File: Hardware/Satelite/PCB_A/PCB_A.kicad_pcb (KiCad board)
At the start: 2 copper layers, 47 x 47 mm, 40 parts, among them J1 Batería LiPo (Soldada), J2 CONUFL001-SMD, J3 Servo Globo, J4 Conector_PCB_A-B, J5 Servo Paracaídas, Q1 SSM3J338R,LF, U1 A2235-H, U2 CC1101RGP, U3 0915BM15A0001E, Y1 26 MHz

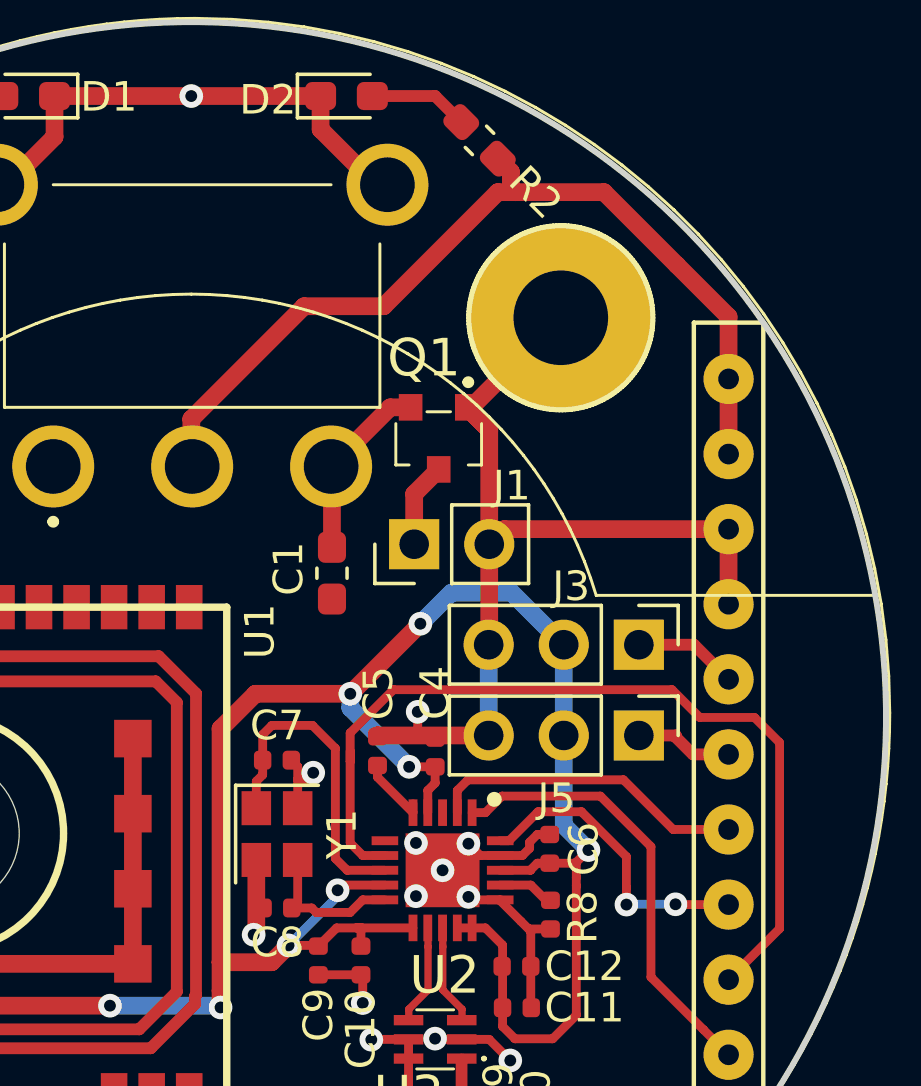
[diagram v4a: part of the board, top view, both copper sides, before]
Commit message: Trazas más gruesas para VBat y corrección de error DRC en PCB_A
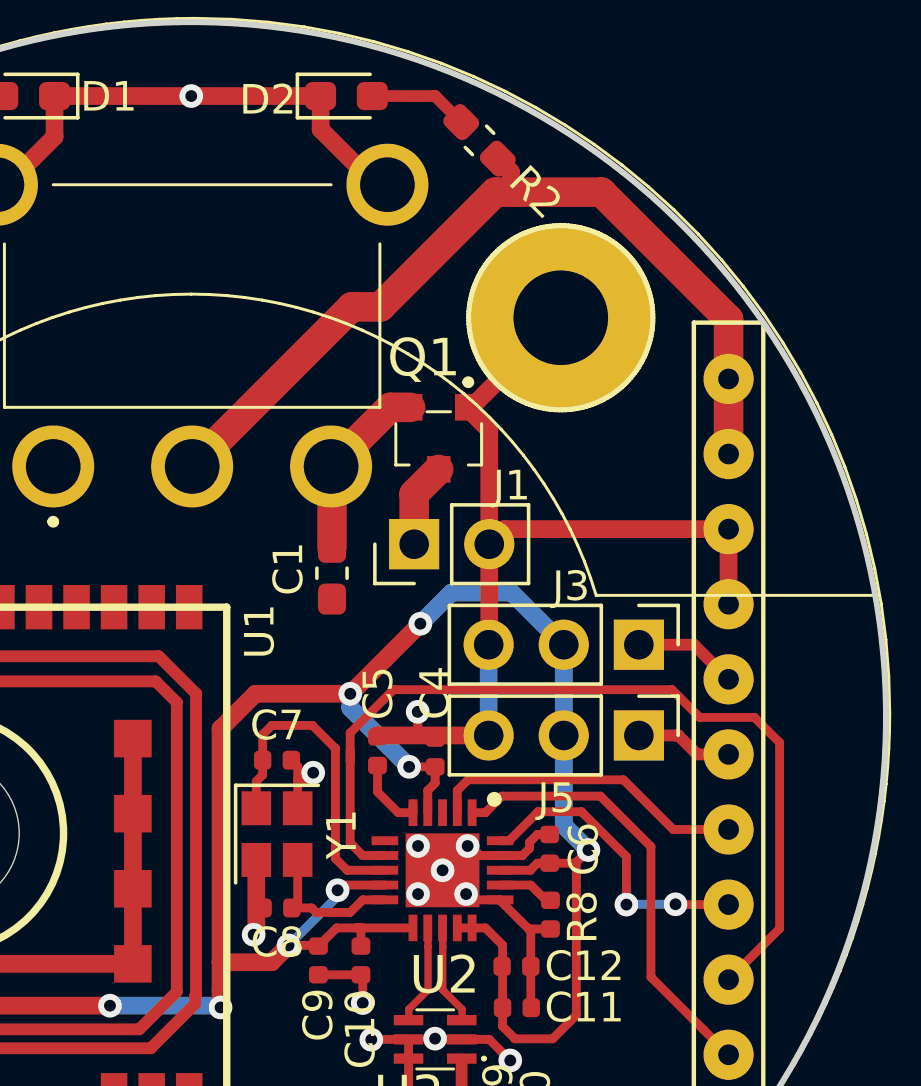
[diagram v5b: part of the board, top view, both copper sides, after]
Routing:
- net Net-(J4-Pad1): track 31.1 -> 29.7 mm
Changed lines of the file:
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@@
     (thickness 1.6)
     (drawings 1)
-    (tracks 332)
+    (tracks 331)
     (zones 0)
     (modules 40)
@@
   )
   (gr_circle (center 0 0) (end 23.5 0) (layer Edge.Cuts) (width 0.2))
-  (segment (start 9.1432 11.5886) (end 9.1432 12.8816) (width 0.4) (layer F.Cu) (net 48))
-  (segment (start 7.3582 9.8886) (end 8.0082 9.2386) (width 0.25) (layer F.Cu) (net 51))
-  (segment (start 8.0082 9.2386) (end 8.0082 7.7732) (width 0.25) (layer F.Cu) (net 51))
-  (segment (start 8.0082 7.7732) (end 8.0082 7.1232) (width 0.25) (layer F.Cu) (net 51))
-  (segment (start 7.3582 10.2636) (end 7.3582 9.8886) (width 0.25) (layer F.Cu) (net 51))
-  (segment (start 8.5082 7.7732) (end 8.5082 7.1232) (width 0.25) (layer F.Cu) (net 52))
-  (segment (start 9.1582 10.2636) (end 9.1582 9.8886) (width 0.25) (layer F.Cu) (net 52))
-  (segment (start 9.1582 9.8886) (end 8.5082 9.2386) (width 0.25) (layer F.Cu) (net 52))
-  (segment (start 8.5082 9.2386) (end 8.5082 7.7732) (width 0.25) (layer F.Cu) (net 52))
   (via (at 8.5 5.19) (size 0.8) (drill 0.4) (layers F.Cu B.Cu) (net 1))
-  (via (at 7.6 6.065) (size 0.8) (drill 0.4) (layers F.Cu B.Cu) (net 1))
-  (via (at 7.6 4.265) (size 0.8) (drill 0.4) (layers F.Cu B.Cu) (net 1))
-  (via (at 9.375 6.09) (size 0.8) (drill 0.4) (layers F.Cu B.Cu) (net 1))
-  (via (at 9.375 4.29) (size 0.8) (drill 0.4) (layers F.Cu B.Cu) (net 1))
+  (via (at 7.6708 5.9944) (size 0.8) (drill 0.4) (layers F.Cu B.Cu) (net 1))
+  (via (at 7.6708 4.3688) (size 0.8) (drill 0.4) (layers F.Cu B.Cu) (net 1))
+  (via (at 9.2964 5.9944) (size 0.8) (drill 0.4) (layers F.Cu B.Cu) (net 1))
+  (via (at 9.3472 4.3688) (size 0.8) (drill 0.4) (layers F.Cu B.Cu) (net 1))
   (segment (start -12.75 -13.25) (end -12.5 -13.5) (width 0.4) (layer F.Cu) (net 1))
   (segment (start -12.75 -7.875) (end -12.75 -13.25) (width 0.4) (layer F.Cu) (net 1))
@@
   (segment (start 5.14 -8.88) (end 4.73 -8.47) (width 0.6) (layer F.Cu) (net 2))
   (segment (start 4.76 -8.44) (end 4.73 -8.47) (width 0.6) (layer F.Cu) (net 2))
-  (segment (start 4.76 -5.735) (end 4.76 -8.44) (width 0.6) (layer F.Cu) (net 2))
-  (segment (start 6.73 -10.47) (end 4.73 -8.47) (width 0.6) (layer F.Cu) (net 2))
-  (segment (start 7.42 -10.47) (end 6.73 -10.47) (width 0.6) (layer F.Cu) (net 2))
+  (segment (start 4.76 -5.735) (end 4.76 -8.44) (width 1) (layer F.Cu) (net 2))
+  (segment (start 6.73 -10.47) (end 4.73 -8.47) (width 1) (layer F.Cu) (net 2))
+  (segment (start 7.42 -10.47) (end 6.73 -10.47) (width 1) (layer F.Cu) (net 2))
   (segment (start -18.175 1.27) (end -16.53 1.27) (width 0.6) (layer F.Cu) (net 3))
   (segment (start -16.53 1.27) (end -15.325 2.475) (width 0.6) (layer F.Cu) (net 3))
@@
   (segment (start 8.25 -21) (end 9.131282 -20.118718) (width 0.4) (layer F.Cu) (net 5))
   (segment (start 6.125 -21) (end 8.25 -21) (width 0.4) (layer F.Cu) (net 5))
-  (segment (start 7.54 -7.54) (end 8.37 -8.37) (width 0.6) (layer F.Cu) (net 6))
-  (segment (start 7.54 -5.84) (end 7.54 -7.54) (width 0.6) (layer F.Cu) (net 6))
+  (segment (start 7.54 -7.54) (end 8.37 -8.37) (width 1) (layer F.Cu) (net 6))
+  (segment (start 7.54 -5.84) (end 7.54 -7.54) (width 1) (layer F.Cu) (net 6))
   (segment (start 17.005 -2.44) (end 15.14 -2.44) (width 0.4) (layer F.Cu) (net 7))
   (segment (start 18.175 -1.27) (end 17.005 -2.44) (width 0.4) (layer F.Cu) (net 7))
@@
   (segment (start 14.62 2.13) (end 16.3 3.81) (width 0.3) (layer F.Cu) (net 16))
   (segment (start 16.39 0.63) (end 15.14 0.63) (width 0.4) (layer F.Cu) (net 17))
-  (segment (start 16.39 0.687081) (end 16.39 0.63) (width 0.4) (layer F.Cu) (net 17))
-  (segment (start 16.972919 1.27) (end 16.39 0.687081) (width 0.4) (layer F.Cu) (net 17))
-  (segment (start 18.175 1.27) (end 16.972919 1.27) (width 0.4) (layer F.Cu) (net 17))
+  (segment (start 16.4796 0.63) (end 16.39 0.63) (width 0.4) (layer F.Cu) (net 17))
+  (segment (start 18.175 1.27) (end 17.1196 1.27) (width 0.4) (layer F.Cu) (net 17))
+  (segment (start 17.1196 1.27) (end 16.4796 0.63) (width 0.4) (layer F.Cu) (net 17))
   (segment (start 5.8 4.69) (end 5.37501 4.26501) (width 0.3) (layer F.Cu) (net 18))
   (segment (start 6.55 4.69) (end 5.8 4.69) (width 0.3) (layer F.Cu) (net 18))
@@
   (segment (start 15.55 4.39) (end 15.55 8.805) (width 0.3) (layer F.Cu) (net 20))
   (segment (start 15.55 8.805) (end 17.325001 10.580001) (width 0.3) (layer F.Cu) (net 20))
-  (segment (start 18.175 -8.89) (end 18.175 -13.535) (width 0.6) (layer F.Cu) (net 21))
-  (segment (start 0 -10.072221) (end 3.817779 -13.89) (width 0.6) (layer F.Cu) (net 21))
-  (segment (start 0 -8.11) (end 0 -10.072221) (width 0.6) (layer F.Cu) (net 21))
-  (segment (start 3.817779 -13.89) (end 6.51 -13.89) (width 0.6) (layer F.Cu) (net 21))
-  (segment (start 6.51 -13.89) (end 10.368718 -17.748718) (width 0.6) (layer F.Cu) (net 21))
-  (segment (start 13.961282 -17.748718) (end 16.43 -15.28) (width 0.6) (layer F.Cu) (net 21))
-  (segment (start 18.175 -13.535) (end 16.43 -15.28) (width 0.6) (layer F.Cu) (net 21))
   (segment (start 10.810659 -17.908059) (end 10.97 -17.748718) (width 0.6) (layer F.Cu) (net 21))
   (segment (start 10.810659 -18.439341) (end 10.810659 -17.908059) (width 0.6) (layer F.Cu) (net 21))
   (segment (start 10.368718 -18.881282) (end 10.810659 -18.439341) (width 0.6) (layer F.Cu) (net 21))
-  (segment (start 10.368718 -17.748718) (end 10.97 -17.748718) (width 0.6) (layer F.Cu) (net 21))
-  (segment (start 10.97 -17.748718) (end 13.961282 -17.748718) (width 0.6) (layer F.Cu) (net 21))
+  (segment (start 13.875284 -17.748718) (end 10.97 -17.748718) (width 1) (layer F.Cu) (net 21))
+  (segment (start 18.175 -13.449002) (end 13.875284 -17.748718) (width 1) (layer F.Cu) (net 21))
+  (segment (start 18.175 -8.89) (end 18.175 -13.449002) (width 1) (layer F.Cu) (net 21))
+  (segment (start 5.4284 -13.8684) (end 0.03 -8.47) (width 1) (layer F.Cu) (net 21))
+  (segment (start 6.4008 -13.8684) (end 5.4284 -13.8684) (width 1) (layer F.Cu) (net 21))
+  (segment (start 10.97 -17.748718) (end 10.281118 -17.748718) (width 1) (layer F.Cu) (net 21))
+  (segment (start 10.281118 -17.748718) (end 6.4008 -13.8684) (width 1) (layer F.Cu) (net 21))
   (segment (start -15.31 14.265) (end -14.6 14.975) (width 0.4) (layer F.Cu) (net 22))
   (segment (start -15.31 12.8) (end -15.31 14.265) (width 0.4) (layer F.Cu) (net 22))
@@
   (segment (start -0.49 -0.49) (end -1.2 -1.2) (width 0.4) (layer F.Cu) (net 29))
   (segment (start 7.5 3.24) (end 7.5 2.94) (width 0.3) (layer F.Cu) (net 41))
-  (segment (start 6.3 1.645) (end 6.3 2.04) (width 0.3) (layer F.Cu) (net 41))
-  (segment (start 6.3 2.04) (end 7.5 3.24) (width 0.3) (layer F.Cu) (net 41))
+  (segment (start 6.9992 3.24) (end 7.5 3.24) (width 0.3) (layer F.Cu) (net 41))
+  (segment (start 6.3 1.645) (end 6.3 2.5408) (width 0.3) (layer F.Cu) (net 41))
+  (segment (start 6.3 2.5408) (end 6.9992 3.24) (width 0.3) (layer F.Cu) (net 41))
   (segment (start 5.275 5.19) (end 6.55 5.19) (width 0.3) (layer F.Cu) (net 42))
   (segment (start 4.875 4.79) (end 5.275 5.19) (width 0.3) (layer F.Cu) (net 42))
@@
   (segment (start 11.485 5.69) (end 12 6.205) (width 0.3) (layer F.Cu) (net 47))
   (segment (start 10.45 5.69) (end 11.485 5.69) (width 0.3) (layer F.Cu) (net 47))
+  (segment (start 9.1432 11.5886) (end 9.1432 12.8816) (width 0.4) (layer F.Cu) (net 48))
+  (segment (start 7.3582 9.8886) (end 8.0082 9.2386) (width 0.25) (layer F.Cu) (net 51))
+  (segment (start 8.0082 9.2386) (end 8.0082 7.7732) (width 0.25) (layer F.Cu) (net 51))
+  (segment (start 8.0082 7.7732) (end 8.0082 7.1232) (width 0.25) (layer F.Cu) (net 51))
+  (segment (start 7.3582 10.2636) (end 7.3582 9.8886) (width 0.25) (layer F.Cu) (net 51))
+  (segment (start 8.5082 7.7732) (end 8.5082 7.1232) (width 0.25) (layer F.Cu) (net 52))
+  (segment (start 9.1582 10.2636) (end 9.1582 9.8886) (width 0.25) (layer F.Cu) (net 52))
+  (segment (start 9.1582 9.8886) (end 8.5082 9.2386) (width 0.25) (layer F.Cu) (net 52))
+  (segment (start 8.5082 9.2386) (end 8.5082 7.7732) (width 0.25) (layer F.Cu) (net 52))
   (zone (net 1) (net_name GND) (layer F.Cu) (hatch edge 0.508)
     (connect_pads (clearance 0.508))

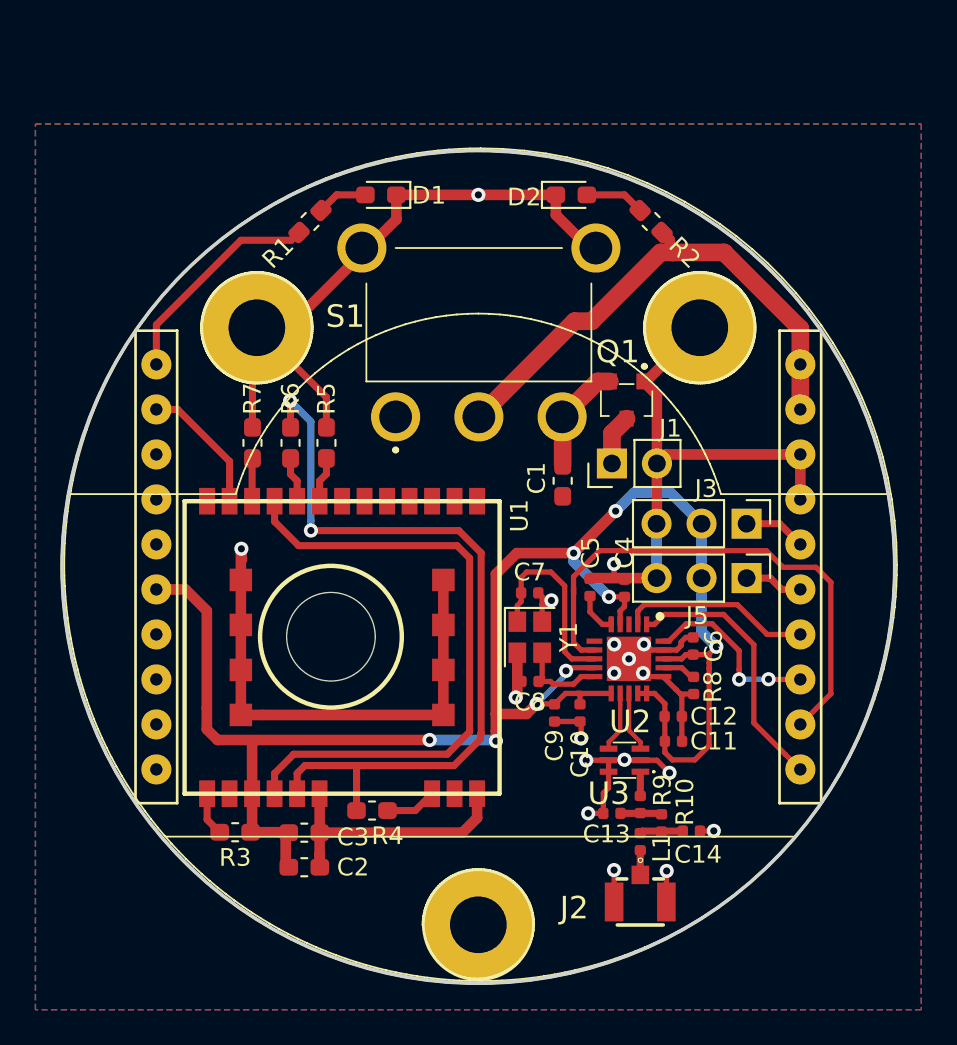
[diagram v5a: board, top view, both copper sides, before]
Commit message: Servos alimentados con 5V internos del conector A-B
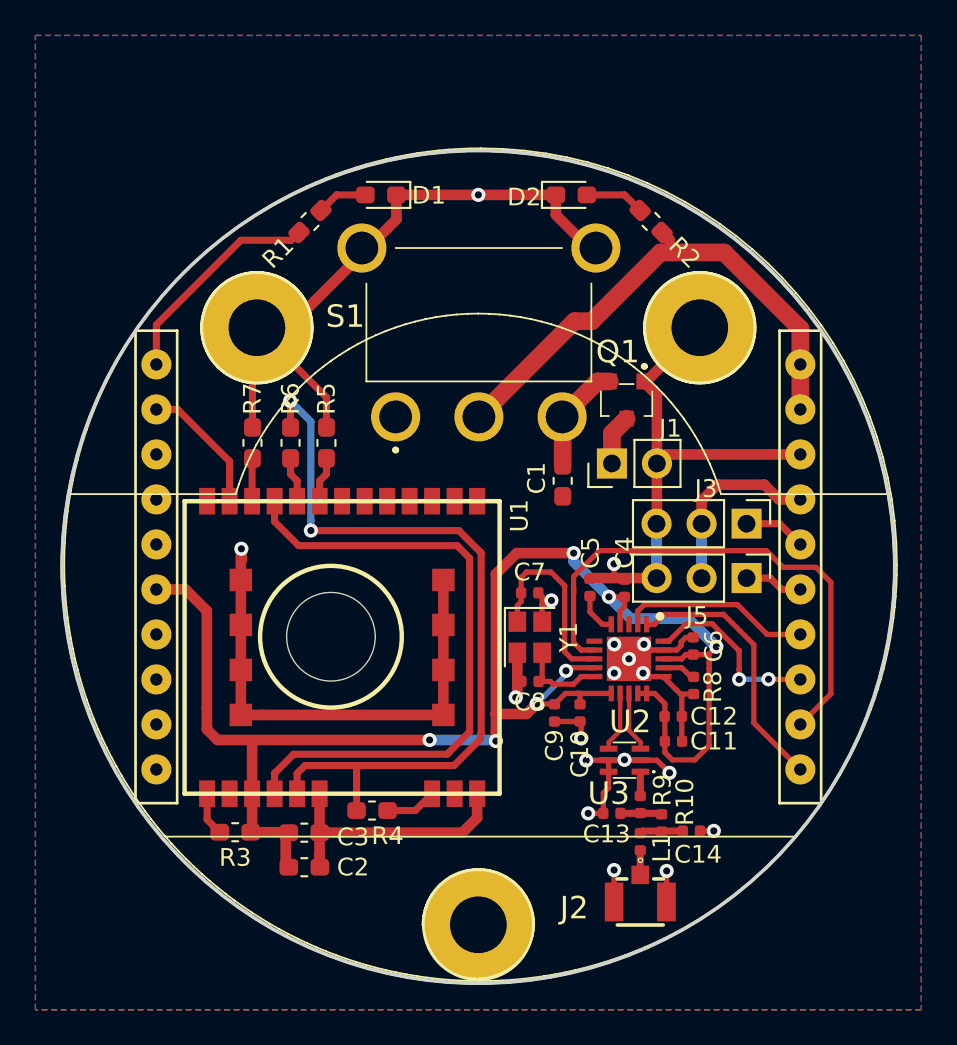
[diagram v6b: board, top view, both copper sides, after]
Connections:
- J3 pad 2: +3V3_Internal -> +5V
- J4 pad 15: Net-(J4-Pad15) -> GND
- J4 pad 4: GND -> +5V
- J5 pad 2: +3V3_Internal -> +5V
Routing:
- net +5V: track 0.00 -> 10.7 mm
- net +3V3_Internal: track 100.7 -> 92.4 mm, vias 8 -> 7
- net GND: track 145.3 -> 142.7 mm

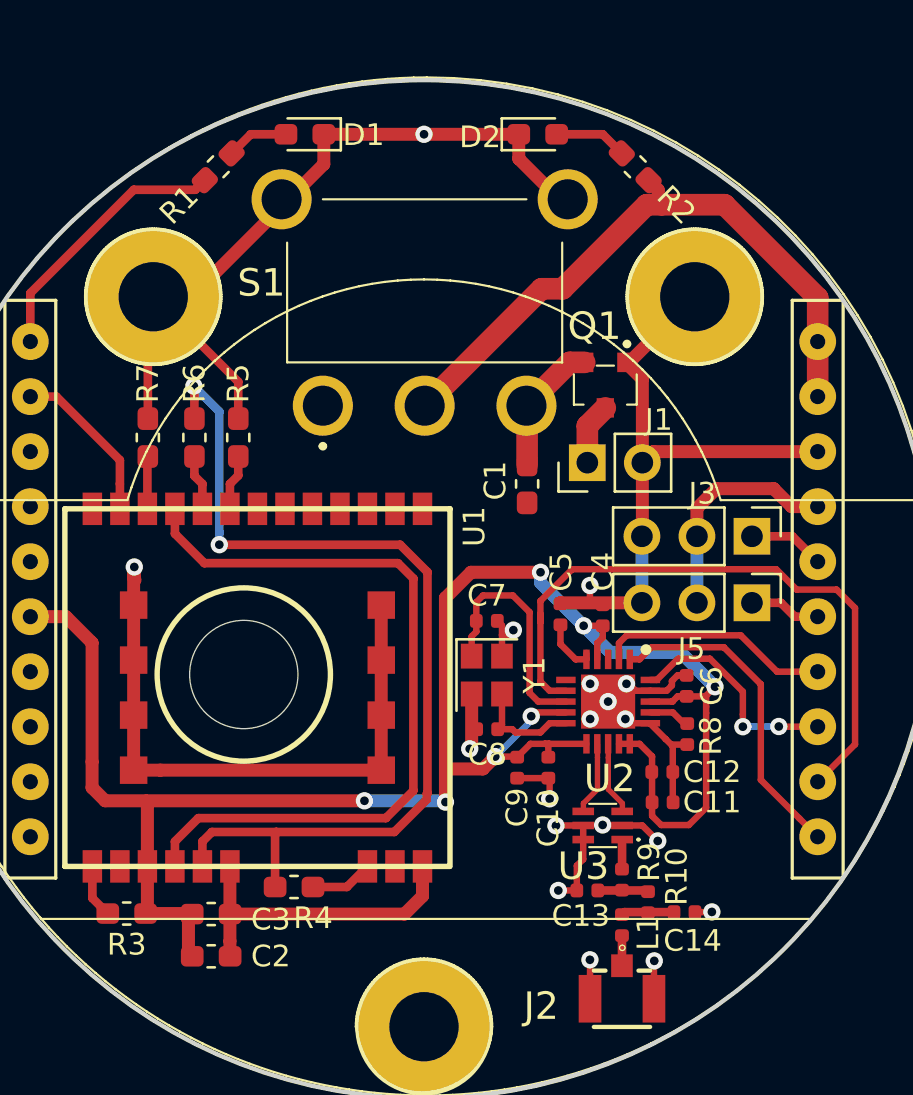
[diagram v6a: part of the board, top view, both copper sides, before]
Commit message: Reducido el díametro de vías de 0.4 a 0.3 en PCB_A
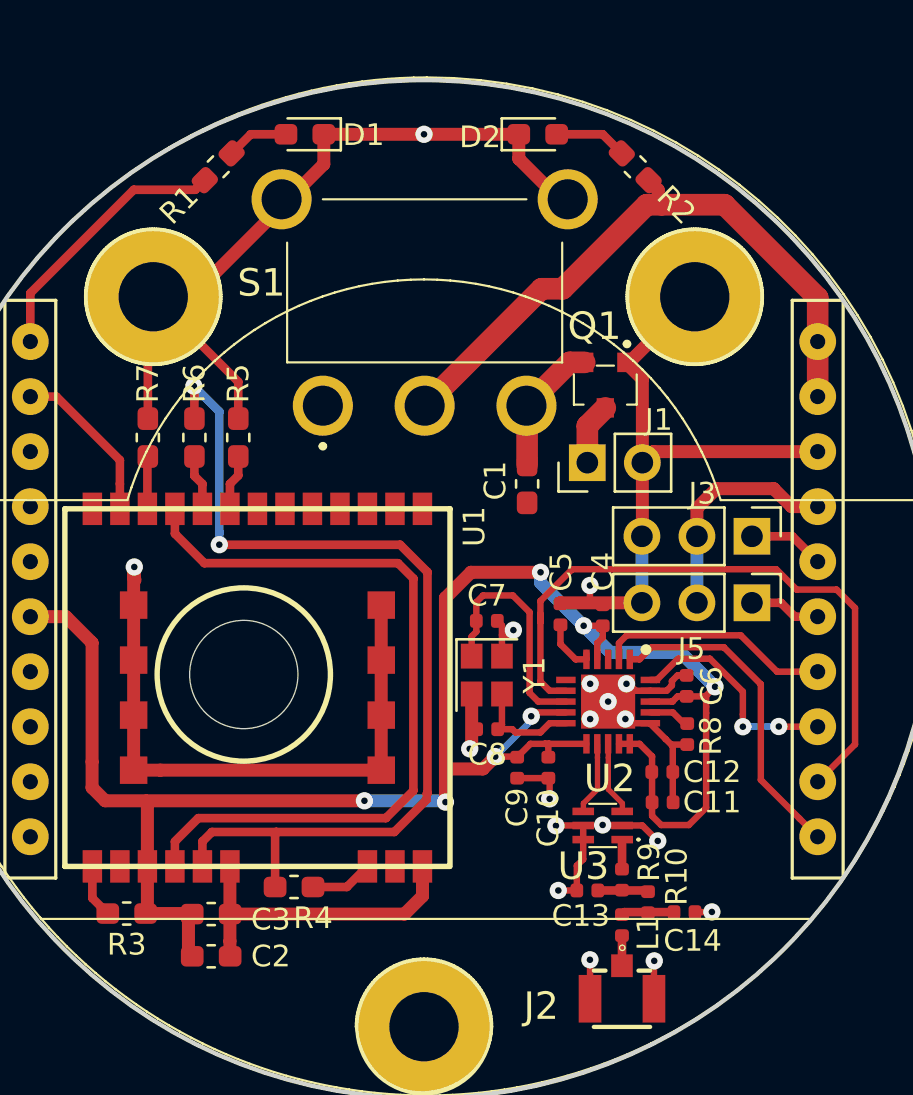
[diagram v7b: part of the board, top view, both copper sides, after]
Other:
- net class ANT: via_drill 0.4 -> 0.3
- net class Alimentacion: via_drill 0.4 -> 0.3
- net class Default: via_drill 0.4 -> 0.3
- net class RF_DIF: via_drill 0.4 -> 0.3

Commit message: PCB_A terminado
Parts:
- added REF**: PCB_mayor_diametro, AXTEC:PCB_mayor_diametro, F.Cu at (0.00, 0.00)
- moved J5 5.79 mm to (20.9, 0.00), turned to 0 degrees
- moved C9 2.82 mm to (6.90, 7.14)
- moved C13 2.82 mm to (10.1, 12.8)
- moved C5 2.82 mm to (8.90, 0.06)
- moved C7 2.82 mm to (5.50, 0.36)
- moved J2 2.82 mm to (11.7, 17.8)
- moved C10 2.82 mm to (8.34, 7.14)
- moved C4 2.82 mm to (10.8, 0.10)
- moved R8 2.82 mm to (14.8, 5.59)
- moved U2 2.82 mm to (11.1, 4.09)
- moved Y1 2.82 mm to (5.50, 2.87)
- moved C11 2.82 mm to (13.6, 8.74)
- moved C12 2.82 mm to (13.6, 7.34)
- moved C14 2.82 mm to (14.6, 13.8)
- moved C6 2.82 mm to (14.7, 3.37)
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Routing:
- net GND: track 142.7 -> 154.8 mm, vias 18 -> 20
- net +5V: track 10.7 -> 20.0 mm
- net +3V3_Internal: track 92.4 -> 98.9 mm
- net /SDI: track 10.4 -> 15.6 mm, vias 2 -> 0
- net /SDO: track 10.8 -> 15.7 mm
- net /GPS_TX: track 7.60 -> 12.5 mm
- net /S_GLOBO: track 3.52 -> 7.37 mm
- net /CS: track 30.4 -> 29.0 mm, vias 0 -> 4
- net /S_PARACAIDAS: track 3.30 -> 4.43 mm
- net /SCLK: track 15.1 -> 15.0 mm, vias 0 -> 2
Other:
- board size 47 x 47 mm -> 54 x 54 mm
- net class Alimentacion: trace_width 0.3 -> 0.6
- net class Default: trace_width 0.3 -> 0.4
